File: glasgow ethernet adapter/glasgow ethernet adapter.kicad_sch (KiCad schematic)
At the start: 57 parts, among them J1 Glasgow Port, J2 RJ45_Amphenol_RJMG201K21120FR, U1 MxL86110, Y1 25 MHz

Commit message: tweaks
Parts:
- added C27: 0.1u, Capacitor_SMD:C_0402_1005Metric, symbol Device:C
- added R24: 0, Resistor_SMD:R_0402_1005Metric, symbol Device:R
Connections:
- net C_GND: now also C27.1, R24.1
- net GND: now also C27.2, R24.2; no longer J1.AXG, J1.BXG
- no-connect marks 4 -> 7
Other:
- moved on the sheet: C22, R10

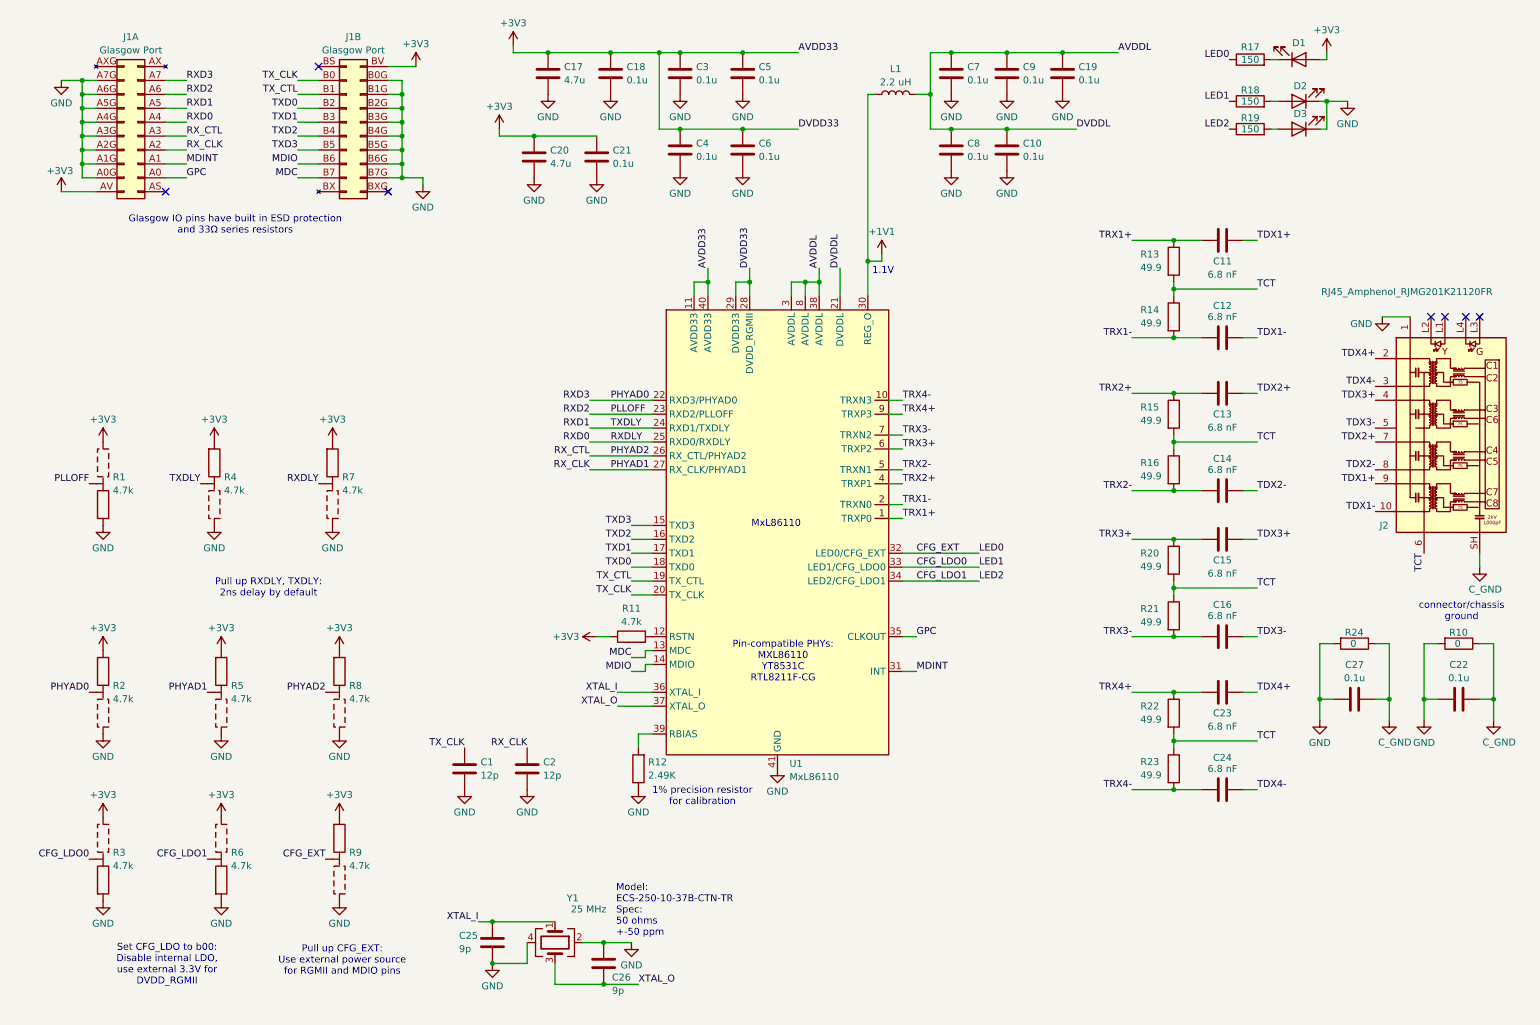
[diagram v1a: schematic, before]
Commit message: swap and re-route pairs
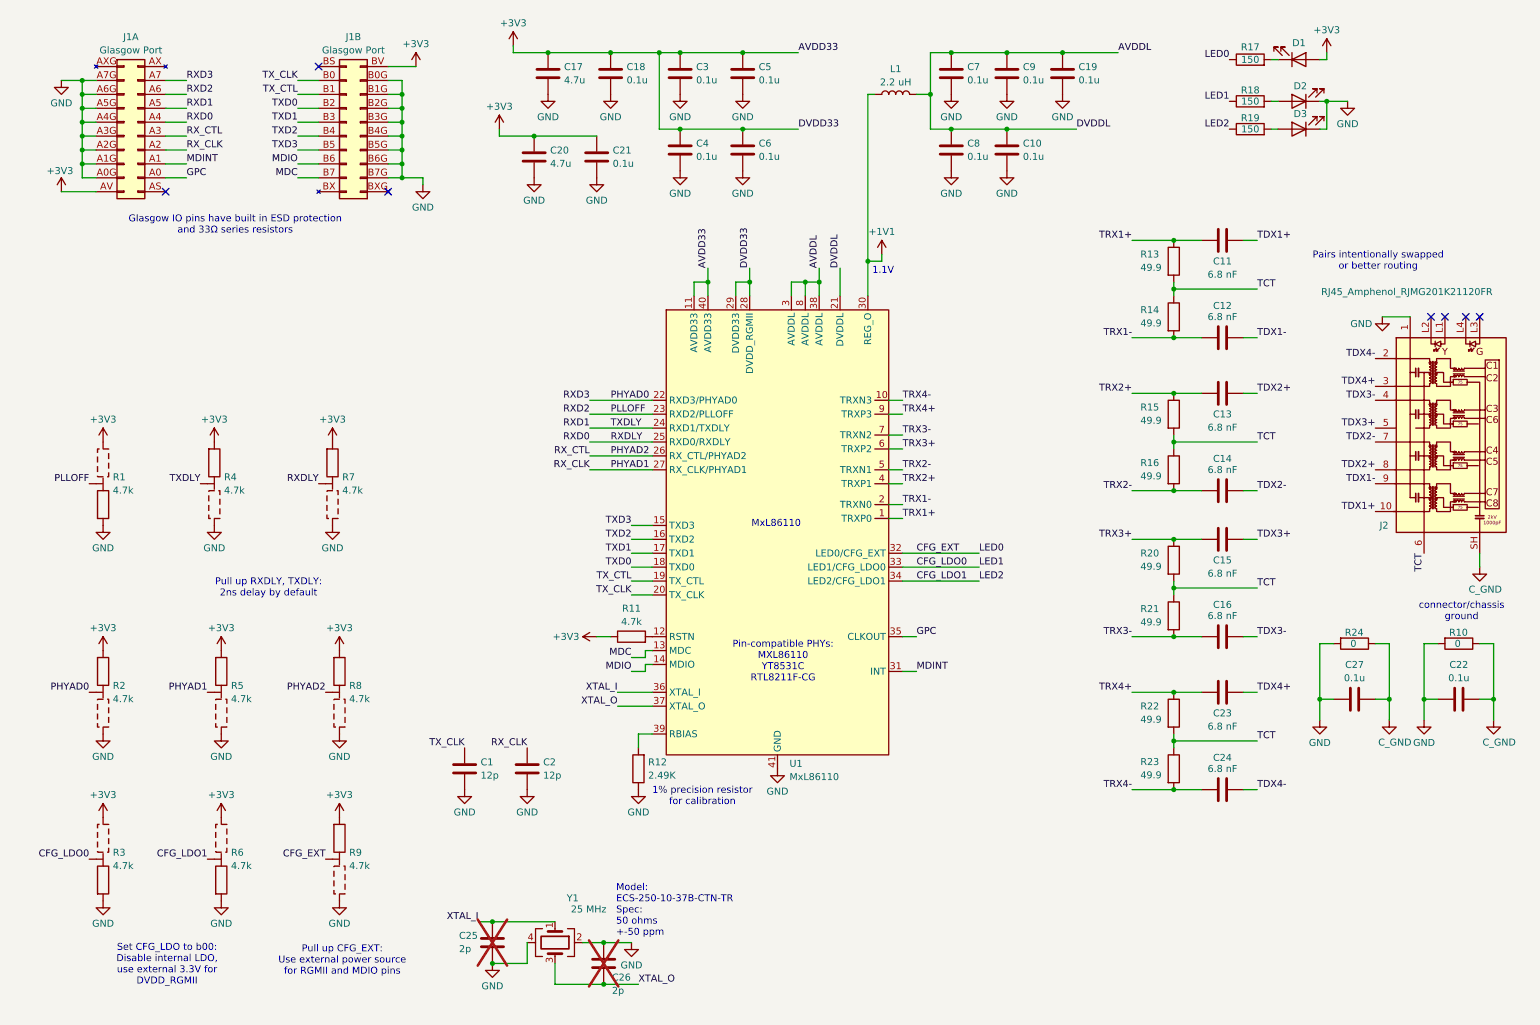
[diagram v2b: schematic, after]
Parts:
- C25, C26: value 9p -> 2p; now not fitted
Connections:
- net TDX1+: now also J2.10 (TD4-); no longer J2.9 (TD4+)
- net TDX1-: now also J2.9 (TD4+); no longer J2.10 (TD4-)
- net TDX2+: now also J2.8 (TD3-); no longer J2.7 (TD3+)
- net TDX2-: now also J2.7 (TD3+); no longer J2.8 (TD3-)
- net TDX3+: now also J2.5 (TD2-); no longer J2.4 (TD2+)
- net TDX3-: now also J2.4 (TD2+); no longer J2.5 (TD2-)
- net TDX4+: now also J2.3 (TD1-); no longer J2.2 (TD1+)
- net TDX4-: now also J2.2 (TD1+); no longer J2.3 (TD1-)
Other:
- note added: "Pairs intentionally swapped or better routing"
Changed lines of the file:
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@@
+		)
+	)
+	(text "Pairs intentionally swapped \nor better routing"
+		(exclude_from_sim no)
+		(at 259.588 58.42 0)
+		(effects
+			(font
+				(size 1.27 1.27)
+			)
 		)
 	)
@@
 	)
 	(label "TDX3+"
-		(at 259.08 83.82 180)
+		(at 259.08 88.9 180)
 		(fields_autoplaced yes)
 		(effects
@@
 	)
 	(label "TDX3-"
-		(at 259.08 88.9 180)
+		(at 259.08 83.82 180)
 		(fields_autoplaced yes)
 		(effects
@@
 	)
 	(label "TDX1+"
-		(at 259.08 99.06 180)
+		(at 259.08 104.14 180)
 		(fields_autoplaced yes)
 		(effects
@@
 	)
 	(label "TDX4-"
-		(at 259.08 81.28 180)
+		(at 259.08 76.2 180)
 		(fields_autoplaced yes)
 		(effects
@@
 	)
 	(label "TDX2+"
-		(at 259.08 91.44 180)
+		(at 259.08 96.52 180)
 		(fields_autoplaced yes)
 		(effects
@@
 	)
 	(label "TDX2-"
-		(at 259.08 96.52 180)
+		(at 259.08 91.44 180)
 		(fields_autoplaced yes)
 		(effects
@@
 	)
 	(label "TDX1-"
-		(at 259.08 104.14 180)
+		(at 259.08 99.06 180)
 		(fields_autoplaced yes)
 		(effects
@@
 	)
 	(label "TDX4+"
-		(at 259.08 76.2 180)
+		(at 259.08 81.28 180)
 		(fields_autoplaced yes)
 		(effects
@@
 		(in_bom yes)
 		(on_board yes)
-		(dnp no)
+		(dnp yes)
 		(property "Reference" "C25"
 			(at 91.694 181.61 0)
@@
 			)
 		)
-		(property "Value" "9p"
+		(property "Value" "2p"
 			(at 91.694 184.0343 0)
 			(effects
@@
 		(in_bom yes)
 		(on_board yes)
-		(dnp no)
+		(dnp yes)
 		(property "Reference" "C26"
 			(at 119.634 189.23 0)
@@
 			)
 		)
-		(property "Value" "9p"
+		(property "Value" "2p"
 			(at 119.634 191.6543 0)
 			(effects

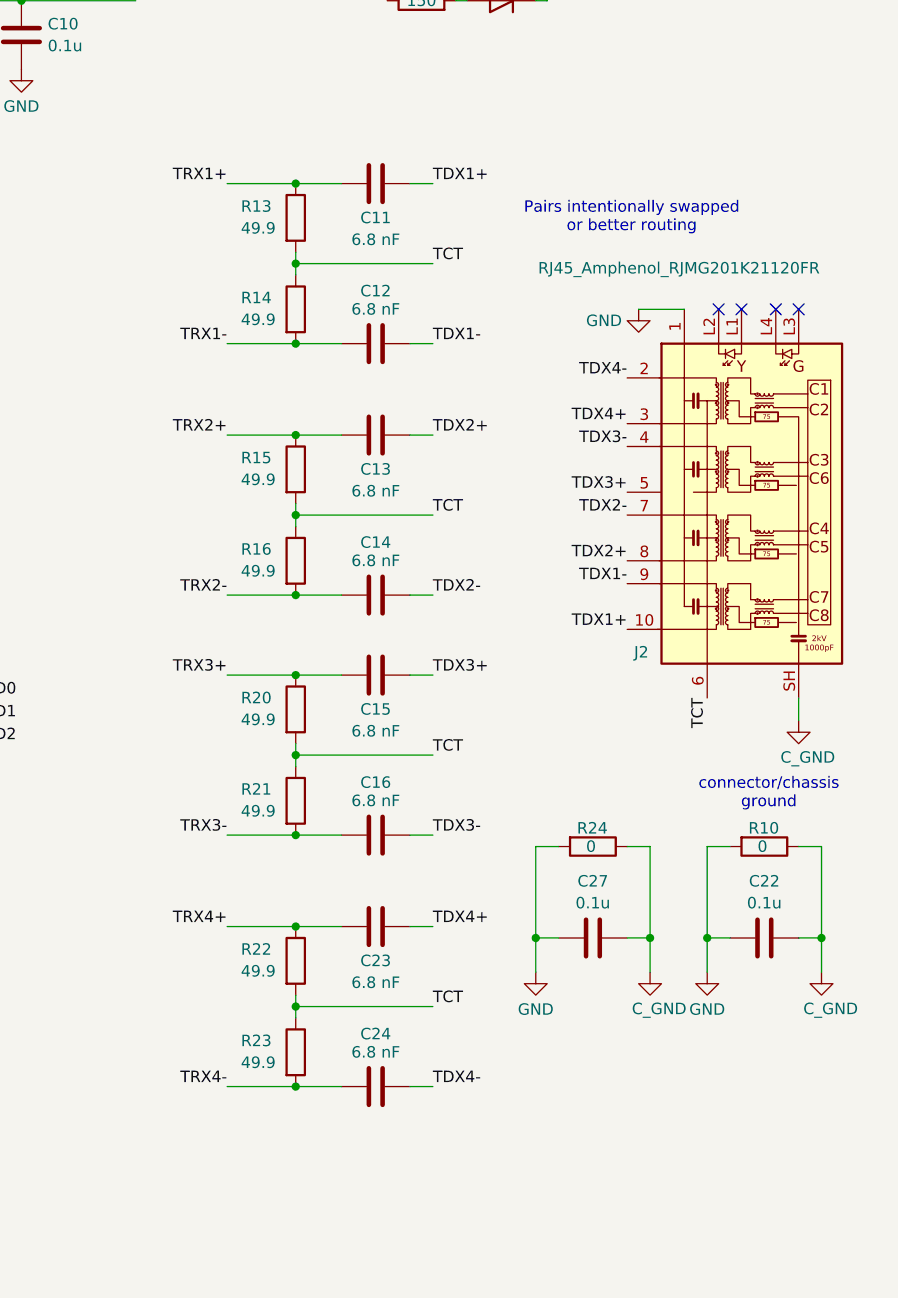
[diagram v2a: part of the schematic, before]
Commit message: simply ground transformer center tap
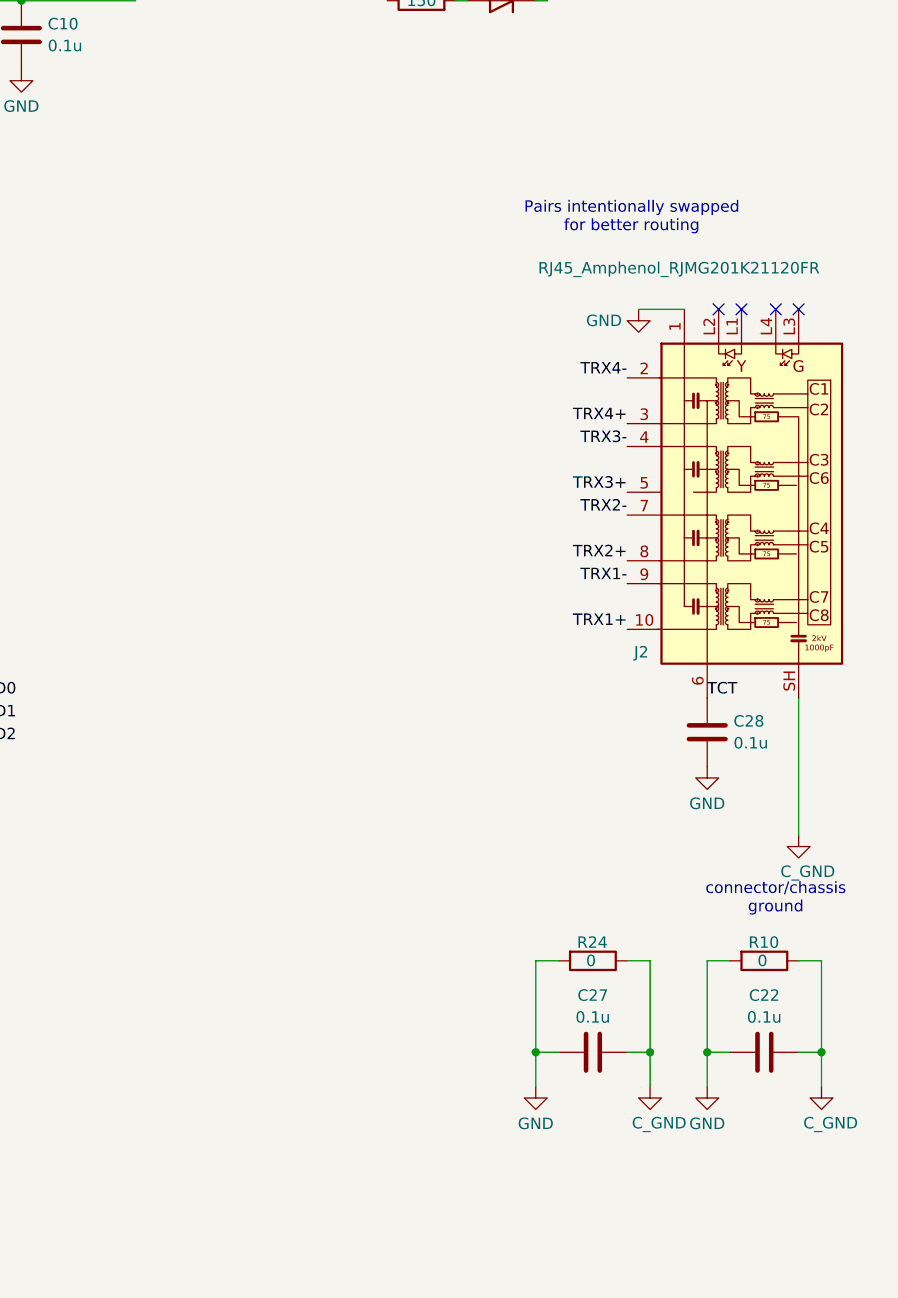
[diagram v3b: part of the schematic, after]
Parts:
- removed C11, C12, C13, C14, C15, C16, C23, C24: 6.8 nF, Capacitor_SMD:C_0402_1005Metric, symbol Device:C
- removed R13, R14, R15, R16, R20, R21, R22, R23: 49.9, Resistor_SMD:R_0402_1005Metric, symbol Device:R
- added C28: 0.1u, Capacitor_SMD:C_0402_1005Metric, symbol Device:C
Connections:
- net TDX1+ is gone; now on net TRX1+: J2.10 (TD4-)
- net TDX1- is gone; now on net TRX1-: J2.9 (TD4+)
- net TDX2+ is gone; now on net TRX2+: J2.8 (TD3-)
- net TDX2- is gone; now on net TRX2-: J2.7 (TD3+)
- net TDX3+ is gone; now on net TRX3+: J2.5 (TD2-)
- net TDX3- is gone; now on net TRX3-: J2.4 (TD2+)
- net TDX4+ is gone; now on net TRX4+: J2.3 (TD1-)
- net TDX4- is gone; now on net TRX4-: J2.2 (TD1+)
- net GND: now also C28.2
- net TCT: now also C28.1
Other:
- note added: "Pairs intentionally swapped for better routing"
- note removed: "Pairs intentionally swapped or better routing"
- moved on the sheet: C22, C27, R10, R24
